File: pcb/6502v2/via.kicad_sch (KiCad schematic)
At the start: 8 parts, among them J4 I/O, J5 Interup Pins, J6 I/O, J7 LDC, J8 Interup Pins, U5 W65C22NxP, U6 W65C22NxP

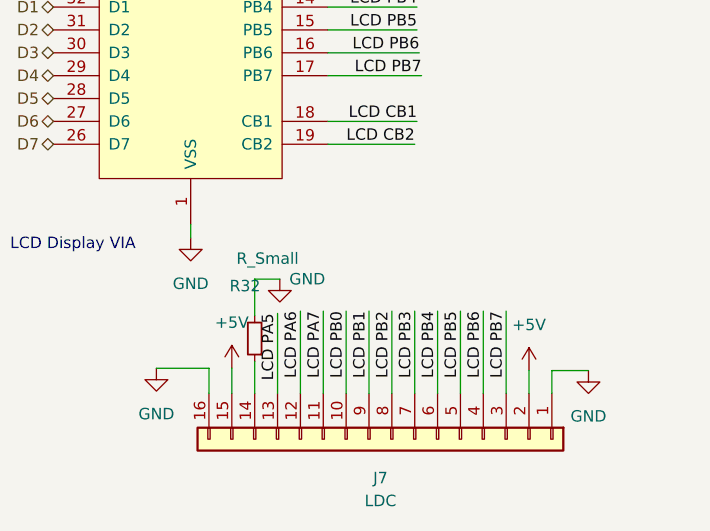
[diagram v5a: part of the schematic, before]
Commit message: Fixed mirrored footprints, updated readme
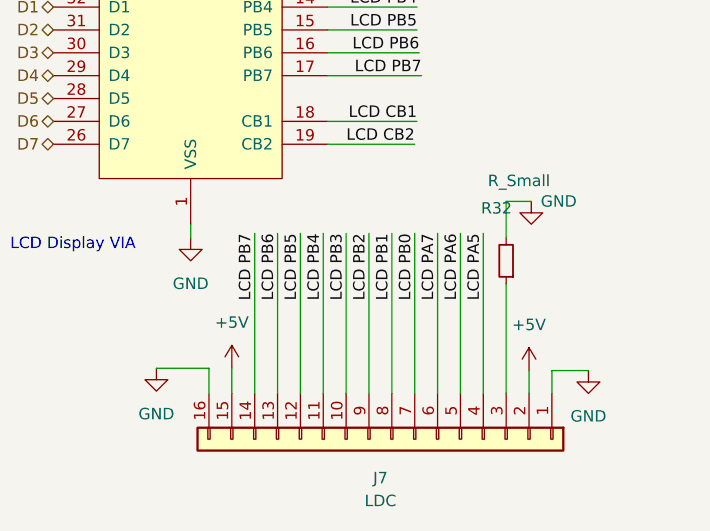
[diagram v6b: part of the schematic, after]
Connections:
- net LCD PA5: now also J7.4 (Pin_4); no longer J7.13 (Pin_13)
- net LCD PA6: now also J7.5 (Pin_5); no longer J7.12 (Pin_12)
- net LCD PA7: now also J7.6 (Pin_6); no longer J7.11 (Pin_11)
- net LCD PB0: now also J7.7 (Pin_7); no longer J7.10 (Pin_10)
- net LCD PB1: now also J7.8 (Pin_8); no longer J7.9 (Pin_9)
- net LCD PB2: now also J7.9 (Pin_9); no longer J7.8 (Pin_8)
- net LCD PB3: now also J7.10 (Pin_10); no longer J7.7 (Pin_7)
- net LCD PB4: now also J7.11 (Pin_11); no longer J7.6 (Pin_6)
- net LCD PB5: now also J7.12 (Pin_12); no longer J7.5 (Pin_5)
- net LCD PB6: now also J7.13 (Pin_13); no longer J7.4 (Pin_4)
- net LCD PB7: now also J7.14 (Pin_14); no longer J7.3 (Pin_3)
- net at R32.1: now also J7.3 (Pin_3); no longer J7.14 (Pin_14)
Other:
- moved on the sheet: R32
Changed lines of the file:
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@@
   (paper "A4")
   (no_connect (at 214.63 77.216))
-  (wire (pts (xy 252.222 144.018) (xy 252.222 153.162))
+  (wire (pts (xy 252.222 135.382) (xy 252.222 153.162))
     (stroke (width 0) (type default) (color 0 0 0 0))
   )
@@
     (stroke (width 0) (type default) (color 0 0 0 0))
   )
-  (wire (pts (xy 236.982 140.462) (xy 239.776 140.462))
+  (wire (pts (xy 264.922 131.826) (xy 267.716 131.826))
     (stroke (width 0) (type default) (color 0 0 0 0))
   )
@@
     (stroke (width 0) (type default) (color 0 0 0 0))
   )
-  (wire (pts (xy 244.602 144.018) (xy 244.602 153.162))
+  (wire (pts (xy 244.602 135.382) (xy 244.602 153.162))
     (stroke (width 0) (type default) (color 0 0 0 0))
   )
@@
     (stroke (width 0) (type default) (color 0 0 0 0))
   )
-  (wire (pts (xy 239.522 144.272) (xy 239.522 153.162))
+  (wire (pts (xy 239.522 135.382) (xy 239.522 153.162))
     (stroke (width 0) (type default) (color 0 0 0 0))
   )
@@
     (stroke (width 0) (type default) (color 0 0 0 0))
   )
-  (wire (pts (xy 264.922 144.018) (xy 264.922 153.162))
+  (wire (pts (xy 264.922 140.97) (xy 264.922 153.162))
     (stroke (width 0) (type default) (color 0 0 0 0))
   )
@@
     (stroke (width 0) (type default) (color 0 0 0 0))
   )
-  (wire (pts (xy 249.682 144.018) (xy 249.682 153.162))
-    (stroke (width 0) (type default) (color 0 0 0 0))
-  )
   (wire (pts (xy 241.046 32.258) (xy 250.952 32.258))
     (stroke (width 0) (type default) (color 0 0 0 0))
@@
     (stroke (width 0) (type default) (color 0 0 0 0))
   )
-  (wire (pts (xy 236.982 149.606) (xy 236.982 153.162))
+  (wire (pts (xy 236.982 135.382) (xy 236.982 153.162))
     (stroke (width 0) (type default) (color 0 0 0 0))
   )
@@
     (stroke (width 0) (type default) (color 0 0 0 0))
   )
-  (wire (pts (xy 247.142 144.018) (xy 247.142 153.162))
-    (stroke (width 0) (type default) (color 0 0 0 0))
-  )
   (wire (pts (xy 241.046 24.638) (xy 250.952 24.638))
     (stroke (width 0) (type default) (color 0 0 0 0))
@@
     (stroke (width 0) (type default) (color 0 0 0 0))
   )
-  (wire (pts (xy 257.302 144.018) (xy 257.302 153.162))
+  (wire (pts (xy 257.302 135.382) (xy 257.302 153.162))
     (stroke (width 0) (type default) (color 0 0 0 0))
   )
@@
     (stroke (width 0) (type default) (color 0 0 0 0))
   )
-  (wire (pts (xy 236.982 144.526) (xy 236.982 140.462))
+  (wire (pts (xy 264.922 135.89) (xy 264.922 131.826))
     (stroke (width 0) (type default) (color 0 0 0 0))
   )
@@
     (stroke (width 0) (type default) (color 0 0 0 0))
   )
-  (wire (pts (xy 242.062 144.018) (xy 242.062 153.162))
+  (wire (pts (xy 242.062 135.382) (xy 242.062 153.162))
     (stroke (width 0) (type default) (color 0 0 0 0))
   )
@@
     (stroke (width 0) (type default) (color 0 0 0 0))
   )
+  (wire (pts (xy 249.682 135.382) (xy 249.682 153.162))
+    (stroke (width 0) (type default) (color 0 0 0 0))
+  )
+  (wire (pts (xy 247.142 135.382) (xy 247.142 153.162))
+    (stroke (width 0) (type default) (color 0 0 0 0))
+  )
   (wire (pts (xy 177.546 107.95) (xy 182.626 107.95))
     (stroke (width 0) (type default) (color 0 0 0 0))
   )
-  (wire (pts (xy 262.382 144.018) (xy 262.382 153.162))
+  (wire (pts (xy 262.382 135.382) (xy 262.382 153.162))
     (stroke (width 0) (type default) (color 0 0 0 0))
   )
@@
     (stroke (width 0) (type default) (color 0 0 0 0))
   )
-  (wire (pts (xy 259.842 144.018) (xy 259.842 153.162))
+  (wire (pts (xy 259.842 135.382) (xy 259.842 153.162))
     (stroke (width 0) (type default) (color 0 0 0 0))
   )
@@
     (stroke (width 0) (type default) (color 0 0 0 0))
   )
-  (wire (pts (xy 254.762 144.018) (xy 254.762 153.162))
+  (wire (pts (xy 254.762 135.382) (xy 254.762 153.162))
     (stroke (width 0) (type default) (color 0 0 0 0))
   )
@@
     (effects (font (size 1.27 1.27)) (justify right bottom))
   )
-  (label "LCD PA5" (at 239.522 144.272 270)
+  (label "LCD PA5" (at 262.382 135.382 270)
     (effects (font (size 1.27 1.27)) (justify right bottom))
   )
@@
     (effects (font (size 1.27 1.27)) (justify right bottom))
   )
-  (label "LCD PB5" (at 259.842 144.018 270)
+  (label "LCD PB5" (at 242.062 135.382 270)
     (effects (font (size 1.27 1.27)) (justify right bottom))
   )
@@
     (effects (font (size 1.27 1.27)) (justify right bottom))
   )
-  (label "LCD PB3" (at 254.762 144.018 270)
-    (effects (font (size 1.27 1.27)) (justify right bottom))
-  )
-  (label "LCD PB6" (at 262.382 144.018 270)
+  (label "LCD PB3" (at 247.142 135.382 270)
+    (effects (font (size 1.27 1.27)) (justify right bottom))
+  )
+  (label "LCD PB6" (at 239.522 135.382 270)
     (effects (font (size 1.27 1.27)) (justify right bottom))
   )
@@
     (effects (font (size 1.27 1.27)) (justify left bottom))
   )
-  (label "LCD PB2" (at 252.222 144.018 270)
+  (label "LCD PB2" (at 249.682 135.382 270)
     (effects (font (size 1.27 1.27)) (justify right bottom))
   )
@@
     (effects (font (size 1.27 1.27)) (justify right bottom))
   )
-  (label "LCD PB0" (at 247.142 144.018 270)
+  (label "LCD PB0" (at 254.762 135.382 270)
     (effects (font (size 1.27 1.27)) (justify right bottom))
   )
@@
     (effects (font (size 1.27 1.27)) (justify right bottom))
   )
-  (label "LCD PB7" (at 264.922 144.018 270)
+  (label "LCD PB7" (at 236.982 135.382 270)
     (effects (font (size 1.27 1.27)) (justify right bottom))
   )
@@
     (effects (font (size 1.27 1.27)) (justify left bottom))
   )
-  (label "LCD PA7" (at 244.602 144.018 270)
+  (label "LCD PA7" (at 257.302 135.382 270)
     (effects (font (size 1.27 1.27)) (justify right bottom))
   )
@@
     (effects (font (size 1.27 1.27)) (justify right bottom))
   )
-  (label "LCD PB1" (at 249.682 144.018 270)
+  (label "LCD PB1" (at 252.222 135.382 270)
     (effects (font (size 1.27 1.27)) (justify right bottom))
   )
@@
     (effects (font (size 1.27 1.27)) (justify left bottom))
   )
-  (label "LCD PA6" (at 242.062 144.018 270)
+  (label "LCD PA6" (at 259.842 135.382 270)
     (effects (font (size 1.27 1.27)) (justify right bottom))
   )
@@
     (effects (font (size 1.27 1.27)) (justify right bottom))
   )
-  (label "LCD PB4" (at 257.302 144.018 270)
+  (label "LCD PB4" (at 244.602 135.382 270)
     (effects (font (size 1.27 1.27)) (justify right bottom))
   )
@@
     (pin "1")
   )
-  (symbol (lib_id "Device:R_Small") (at 236.982 147.066 180) (unit 1)
+  (symbol (lib_id "Device:R_Small") (at 264.922 138.43 180) (unit 1)
     (in_bom yes) (on_board yes)
-    (property "Reference" "R32" (id 0) (at 234.188 141.224 0)
+    (property "Reference" "R32" (id 0) (at 262.128 132.588 0)
       (effects (font (size 1.27 1.27)) (justify right))
     )
-    (property "Value" "R_Small" (id 1) (at 234.95 138.176 0)
+    (property "Value" "R_Small" (id 1) (at 262.89 129.54 0)
       (effects (font (size 1.27 1.27)) (justify right))
     )
-    (property "Footprint" "Resistor_SMD:R_0805_2012Metric" (id 2) (at 236.982 147.066 0)
-      (effects (font (size 1.27 1.27)) hide)
-    )
-    (property "Datasheet" "~" (id 3) (at 236.982 147.066 0)
+    (property "Footprint" "Resistor_SMD:R_0805_2012Metric" (id 2) (at 264.922 138.43 0)
+      (effects (font (size 1.27 1.27)) hide)
+    )
+    (property "Datasheet" "~" (id 3) (at 264.922 138.43 0)
       (effects (font (size 1.27 1.27)) hide)
     )
@@
     (pin "4")
   )
-  (symbol (lib_id "power:GND") (at 239.776 140.462 0) (unit 1)
+  (symbol (lib_id "power:GND") (at 267.716 131.826 0) (unit 1)
     (in_bom yes) (on_board yes)
-    (property "Reference" "#PWR044" (id 0) (at 239.776 146.812 0)
-      (effects (font (size 1.27 1.27)) hide)
-    )
-    (property "Value" "GND" (id 1) (at 242.824 140.462 0))
-    (property "Footprint" "" (id 2) (at 239.776 140.462 0)
-      (effects (font (size 1.27 1.27)) hide)
-    )
-    (property "Datasheet" "" (id 3) (at 239.776 140.462 0)
-      (effects (font (size 1.27 1.27)) hide)
-    )
+    (property "Reference" "#PWR044" (id 0) (at 267.716 138.176 0)
+      (effects (font (size 1.27 1.27)) hide)
+    )
+    (property "Value" "GND" (id 1) (at 270.764 131.826 0))
+    (property "Footprint" "" (id 2) (at 267.716 131.826 0)
+      (effects (font (size 1.27 1.27)) hide)
+    )
+    (property "Datasheet" "" (id 3) (at 267.716 131.826 0)
+      (effects (font (size 1.27 1.27)) hide)
+    )
